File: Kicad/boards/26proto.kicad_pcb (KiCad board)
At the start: 2 copper layers, 17 parts, among them J2 Micro_SD_Card, J3 Conn_01x04, J4 Conn_01x04, U1 MOUDLE-SEEEDUINO-XIAO-ESP32C3, U2 MAX3485, U4 MAX3485, U6 MAX3485, U9 MAX3485

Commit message: update sch
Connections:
- U1 pad 3: unconnected-(U1-GPIO4_A2_D2-Pad3) -> RES
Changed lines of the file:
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@@
 	(net 14 "Pot_trim")
 	(net 15 "SDA_board3")
-	(net 16 "unconnected-(U1-GPIO4_A2_D2-Pad3)")
+	(net 16 "RES")
 	(net 17 "unconnected-(U1-MTDI-Pad17)")
 	(net 18 "SDA-MOSI")
@@
 			(layers "F.Cu" "F.Mask" "F.Paste")
 			(roundrect_rratio 0.25)
-			(net 16 "unconnected-(U1-GPIO4_A2_D2-Pad3)")
+			(net 16 "RES")
 			(pinfunction "GPIO4_A2_D2")
-			(pintype "passive+no_connect")
+			(pintype "passive")
 			(thermal_bridge_angle 45)
 		)

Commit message: updated sch
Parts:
- added J1: 5051104096, footprints:CON_5051104096_MOL, F.Cu at (108.5, 62.8)
- added U11: MOUDLE-SEEEDUINO-XIAO-ESP32C3, footprints:XIAO-ESP32C3-SMD, F.Cu at (62.3, 12.8)
- added U5: MOUDLE-SEEEDUINO-XIAO-ESP32C3, footprints:XIAO-ESP32C3-SMD, F.Cu at (22.2, 12.8)
- added U7: MOUDLE-SEEEDUINO-XIAO-ESP32C3, footprints:XIAO-ESP32C3-SMD, F.Cu at (42.2, 12.8)
- J2: footprint Connector_Card:microSD_HC_Hirose_DM3D-SF -> Connector_Card:microSD_HC_Hirose_DM3AT-SF-PEJM5
- J4: footprint Connector_JST:JST_XH_B3B-XH-A_1x03_P2.50mm_Vertical -> Connector_JST:JST_XH_B4B-XH-A_1x04_P2.50mm_Vertical
- U1: footprint RF_Module:MCU_Seeed_ESP32C3 -> footprints:XIAO-ESP32C3-SMD
- U10: footprint Connector_PinHeader_2.54mm:PinHeader_1x07_P2.54mm_Vertical -> Connector_JST:JST_XH_B7B-XH-A_1x07_P2.50mm_Vertical
- U8: footprint Connector_PinHeader_2.54mm:PinHeader_1x06_P2.54mm_Vertical -> Connector_JST:JST_XH_B6B-XH-A_1x06_P2.50mm_Vertical
- moved U10 21.0 mm to (53.0, 72.5)
- moved J2 18.3 mm to (36.5, 68.5)
- moved U1 10.4 mm to (45.5, 40.0)
- moved U8 7.90 mm to (98.0, 37.0)

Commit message: edited pcb
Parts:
- added J5: RS485_TFT, Connector_JST:JST_XH_S4B-XH-SM4-TB_1x04-1MP_P2.50mm_Horizontal, F.Cu at (134.4, 23.4)
- added J6: RS485_airdata, Connector_JST:JST_XH_S4B-XH-SM4-TB_1x04-1MP_P2.50mm_Horizontal, F.Cu at (134.4, 36.5)
- added J7: RS485_logger_2, Connector_JST:JST_XH_S4B-XH-SM4-TB_1x04-1MP_P2.50mm_Horizontal, F.Cu at (130.5, 134.0)
- added J8: RS485_logger, Connector_JST:JST_XH_S4B-XH-SM4-TB_1x04-1MP_P2.50mm_Horizontal, F.Cu at (127.5, 98.5)
- added J9: BNO085, footprints:MODULE_4754, F.Cu at (108.1, 128.3)
- added R4: R, Resistor_SMD:R_0201_0603Metric_Pad0.64x0.40mm_HandSolder, F.Cu at (144.7, 17.8)
- added R5: R, Resistor_SMD:R_0201_0603Metric_Pad0.64x0.40mm_HandSolder, F.Cu at (144.7, 19.6)
- AS5600: renamed from U8; value ~ -> AS5600 breakout board; footprint Connector_JST:JST_XH_B6B-XH-A_1x06_P2.50mm_Vertical -> Connector_PinHeader_2.54mm:PinHeader_1x06_P2.54mm_Vertical
- DPS310: renamed from U10; value ~ -> Adafruit DPS310; footprint Connector_JST:JST_XH_B7B-XH-A_1x07_P2.50mm_Vertical -> Connector_PinHeader_2.54mm:PinHeader_1x07_P2.54mm_Vertical
- J3: value Conn_01x04 -> URM37; footprint Connector_JST:JST_XH_B4B-XH-A_1x04_P2.50mm_Vertical -> Connector_JST:JST_XH_S4B-XH-SM4-TB_1x04-1MP_P2.50mm_Horizontal
- J4: value Conn_01x04 -> RE12A; footprint Connector_JST:JST_XH_B4B-XH-A_1x04_P2.50mm_Vertical -> Connector_JST:JST_XH_S4B-XH-SM4-TB_1x04-1MP_P2.50mm_Horizontal
- RV1, RV2, RV3: footprint Connector_JST:JST_XH_B3B-XH-A_1x03_P2.50mm_Vertical -> Connector_JST:JST_XH_S3B-XH-SM4-TB_1x03-1MP_P2.50mm_Horizontal
- U1: value MOUDLE-SEEEDUINO-XIAO-ESP32C3 -> MOUDLE-SEEEDUINO-XIAO-ESP32C3_TFT
- U11: value MOUDLE-SEEEDUINO-XIAO-ESP32C3 -> MOUDLE-SEEEDUINO-XIAO-ESP32C3_pot
- U5: value MOUDLE-SEEEDUINO-XIAO-ESP32C3 -> MOUDLE-SEEEDUINO-XIAO-ESP32C3_logger
- U7: value MOUDLE-SEEEDUINO-XIAO-ESP32C3 -> MOUDLE-SEEEDUINO-XIAO-ESP32C3_airdata
- moved RV3 148.1 mm to (218.8, 54.5)
- moved J3 142.0 mm to (212.8, 37.2)
- moved U11 132.2 mm to (192.0, 38.5)
- moved RV2 132.2 mm to (203.0, 57.5)
- moved U7 131.2 mm to (171.0, 38.0)
- moved U5 125.0 mm to (107.3, 104.4)
- moved RV1 117.3 mm to (187.5, 58.5)
- moved J2 105.4 mm to (129.5, 118.0), turned to 90 degrees
- moved J1 55.7 mm to (163.5, 54.5), turned to 180 degrees
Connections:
- AS5600 pad 1: (no net) -> unconnected-(AS5600-5V-Pad1)
- AS5600 pad 2: (no net) -> +3.3V
- AS5600 pad 3: (no net) -> GND
- AS5600 pad 4: (no net) -> SCL_airdata
- AS5600 pad 5: (no net) -> SDA_aridata
- AS5600 pad 6: (no net) -> unconnected-(AS5600-OUT-Pad6)
- DPS310 pad 1: (no net) -> unconnected-(DPS310-VIN-Pad1)
- DPS310 pad 2: (no net) -> +3.3V
- DPS310 pad 3: (no net) -> GND
- DPS310 pad 4: (no net) -> SCL_airdata
- DPS310 pad 5: (no net) -> GND
- DPS310 pad 6: (no net) -> SDA_aridata
- DPS310 pad 7: (no net) -> +3.3V
- U11 pad 11: Net-(U11-GPIO10_D10_MOSI) -> unconnected-(U11-GPIO10_D10_MOSI-Pad11)
- U11 pad 7: Net-(U11-GPIO21_D6_TX) -> unconnected-(U11-GPIO21_D6_TX-Pad7)
- U11 pad 8: Net-(U11-GPIO20_D7_RX) -> unconnected-(U11-GPIO20_D7_RX-Pad8)

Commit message: edited sch and pcb
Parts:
- added Q2: NPN, Package_TO_SOT_SMD:SOT-23, F.Cu at (126.6, 79.0)
- added R6: R, Resistor_SMD:R_0201_0603Metric_Pad0.64x0.40mm_HandSolder, F.Cu at (43.6, 104.5)
- added R7: R, Resistor_SMD:R_0201_0603Metric_Pad0.64x0.40mm_HandSolder, F.Cu at (43.6, 106.2)
- added R8: R, Resistor_SMD:R_0201_0603Metric_Pad0.64x0.40mm_HandSolder, F.Cu at (43.6, 108.0)
- moved J6 103.4 mm to (57.5, 105.5), turned to 180 degrees
- moved R4 82.6 mm to (65.6, 41.5)
- moved C1 75.7 mm to (119.1, 105.0)
- moved R1 75.7 mm to (119.1, 106.8)
- moved R2 75.7 mm to (119.1, 108.5)
- moved R3 75.7 mm to (119.1, 110.2)
- moved AS5600 72.0 mm to (43.0, 83.4)
- moved J5 54.6 mm to (168.1, 66.5), turned to 180 degrees
- moved U1 48.8 mm to (57.0, 87.4), turned to -90 degrees
- moved R5 35.2 mm to (153.9, 53.5)
- moved J3 34.1 mm to (231.0, 66.0), turned to 180 degrees
- moved J4 31.6 mm to (57.0, 66.5)
- moved DPS310 14.6 mm to (43.0, 61.9)
- moved RV3 12.6 mm to (214.5, 66.2), turned to 180 degrees
- moved J1 10.0 mm to (173.5, 55.5), turned to 0 degrees
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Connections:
- AS5600 pad 2: +3.3V -> encoder_anode
- AS5600 pad 3: GND -> encoder_cathode
- C1 pad 1: +3.3V -> encoder_anode
- C1 pad 2: GND -> encoder_cathode
- DPS310 pad 2: +3.3V -> encoder_anode
- DPS310 pad 3: GND -> encoder_cathode
- DPS310 pad 5: GND -> encoder_cathode
- DPS310 pad 7: +3.3V -> encoder_anode
- J1 pad 1: GND -> encoder_cathode
- J1 pad 31: GND -> encoder_cathode
- J1 pad 32: +3.3V -> encoder_anode
- J1 pad 33: +3.3V -> encoder_anode
- J1 pad 34: GND -> encoder_cathode
- J1 pad 35: GND -> encoder_cathode
- J1 pad 36: GND -> encoder_cathode
- J1 pad 37: GND -> encoder_cathode
- J1 pad 39: GND -> encoder_cathode
- J1 pad 7: +3.3V -> encoder_anode
- J1 pad 8: +3.3V -> encoder_anode
- J2 pad 4: +3.3V -> encoder_anode
- J2 pad 6: GND -> encoder_cathode
- J2 pad 9: GND -> encoder_cathode
- J3 pad 1: +3.3V -> encoder_anode
- J3 pad 2: GND -> encoder_cathode
- J4 pad 1: +3.3V -> Net-(J4-Pin_1)
- J4 pad 2: GND -> encoder_raw
- J4 pad 3: Encoder_Apin -> encoder_cathode
- J4 pad 4: Encoder_Bpin -> encoder_cathode
- J5 pad 2: GND -> encoder_cathode
- J6 pad 2: GND -> encoder_cathode
- J7 pad 2: GND -> encoder_cathode
- J8 pad 2: GND -> encoder_cathode
- R1 pad 2: +3.3V -> encoder_anode
- R2 pad 2: +3.3V -> encoder_anode
- R3 pad 2: +3.3V -> encoder_anode
- RV1 pad 1: GND -> encoder_cathode
- RV1 pad 3: +3.3V -> encoder_anode
- RV2 pad 1: GND -> encoder_cathode
- RV2 pad 3: +3.3V -> encoder_anode
- RV3 pad 1: GND -> encoder_cathode
- RV3 pad 3: +3.3V -> encoder_anode
- U1 pad 12: +3.3V -> encoder_anode
- U1 pad 13: GND -> encoder_cathode
- U1 pad 16: GND -> encoder_cathode
- U11 pad 12: +3.3V -> encoder_anode
- U11 pad 13: GND -> encoder_cathode
- U11 pad 16: GND -> encoder_cathode
- U2 pad 5: GND -> encoder_cathode
- U2 pad 8: +3.3V -> encoder_anode
- U4 pad 5: GND -> encoder_cathode
- U4 pad 8: +3.3V -> encoder_anode
- U5 pad 12: +3.3V -> encoder_anode
- U5 pad 13: GND -> encoder_cathode
- U5 pad 16: GND -> encoder_cathode
- U6 pad 5: GND -> encoder_cathode
- U6 pad 8: +3.3V -> encoder_anode
- U7 pad 10: Encoder_Apin -> encoder_out
- U7 pad 12: +3.3V -> encoder_anode
- U7 pad 13: GND -> encoder_cathode
- U7 pad 16: GND -> encoder_cathode
- U7 pad 9: Encoder_Bpin -> unconnected-(U7-GPIO8_D8_SCK-Pad9)

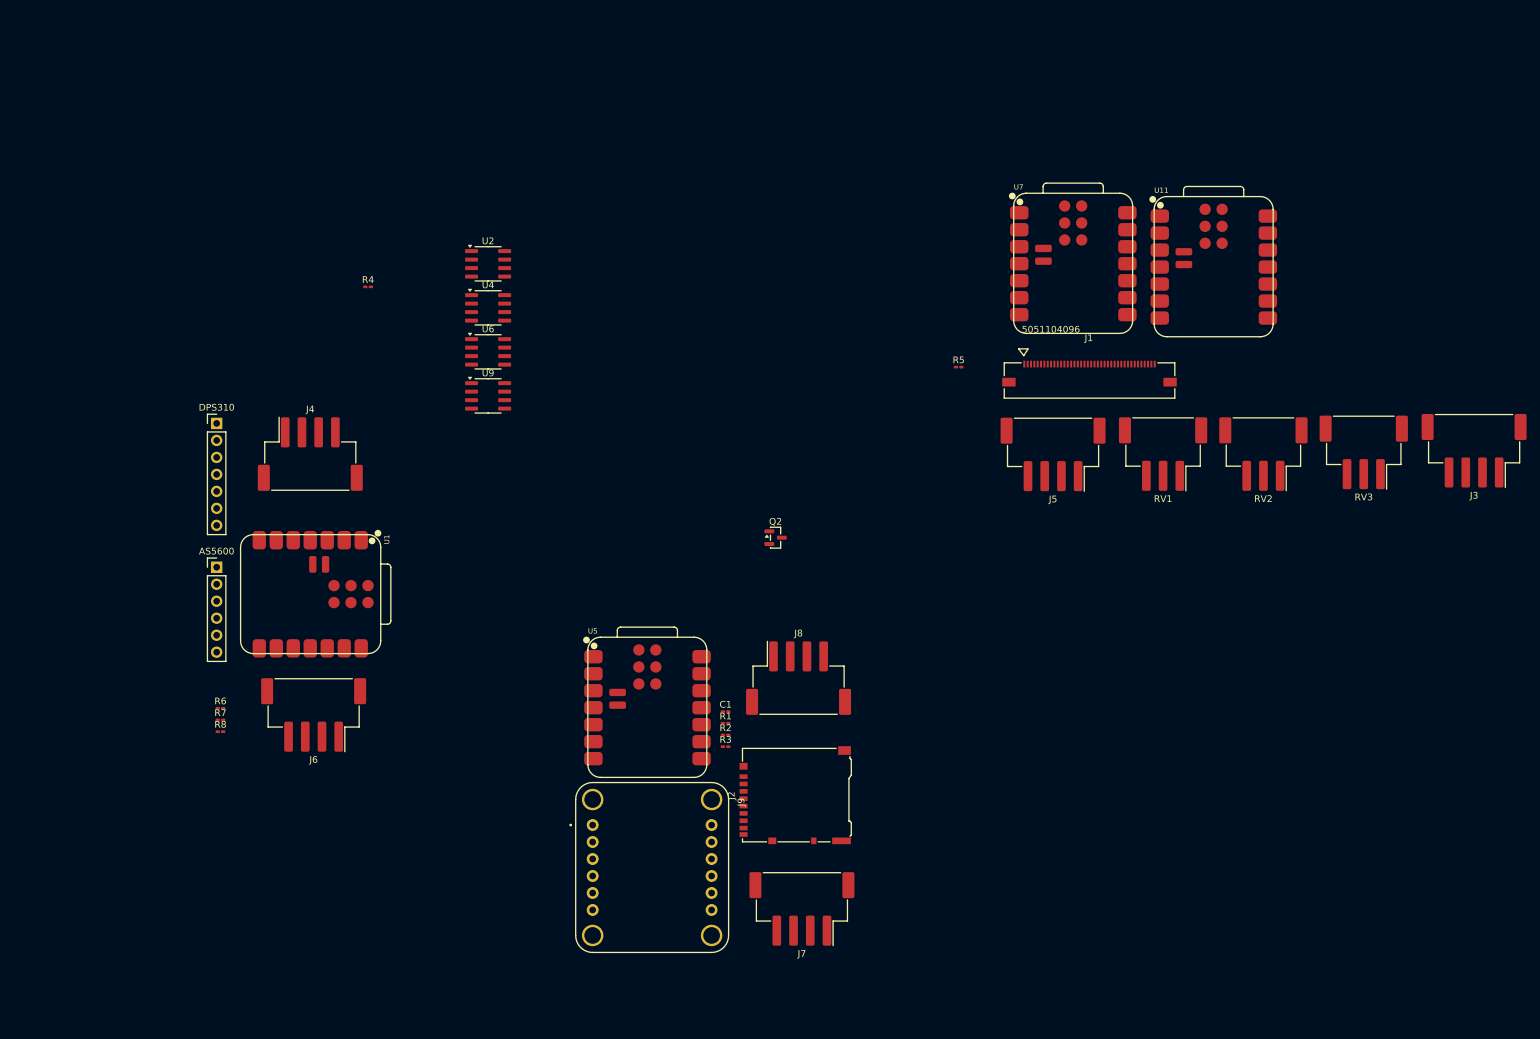
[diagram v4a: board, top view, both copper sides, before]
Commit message: Add battery connector and update net assignments
Added Batt1 JST PH connector footprint and R4 resistor for RS485 lines. Updated net assignments for U11 pins, replaced encoder_anode with +3.3V and pot_Vin where appropriate, and made related schematic and PCB changes. Also added a backup ZIP file.
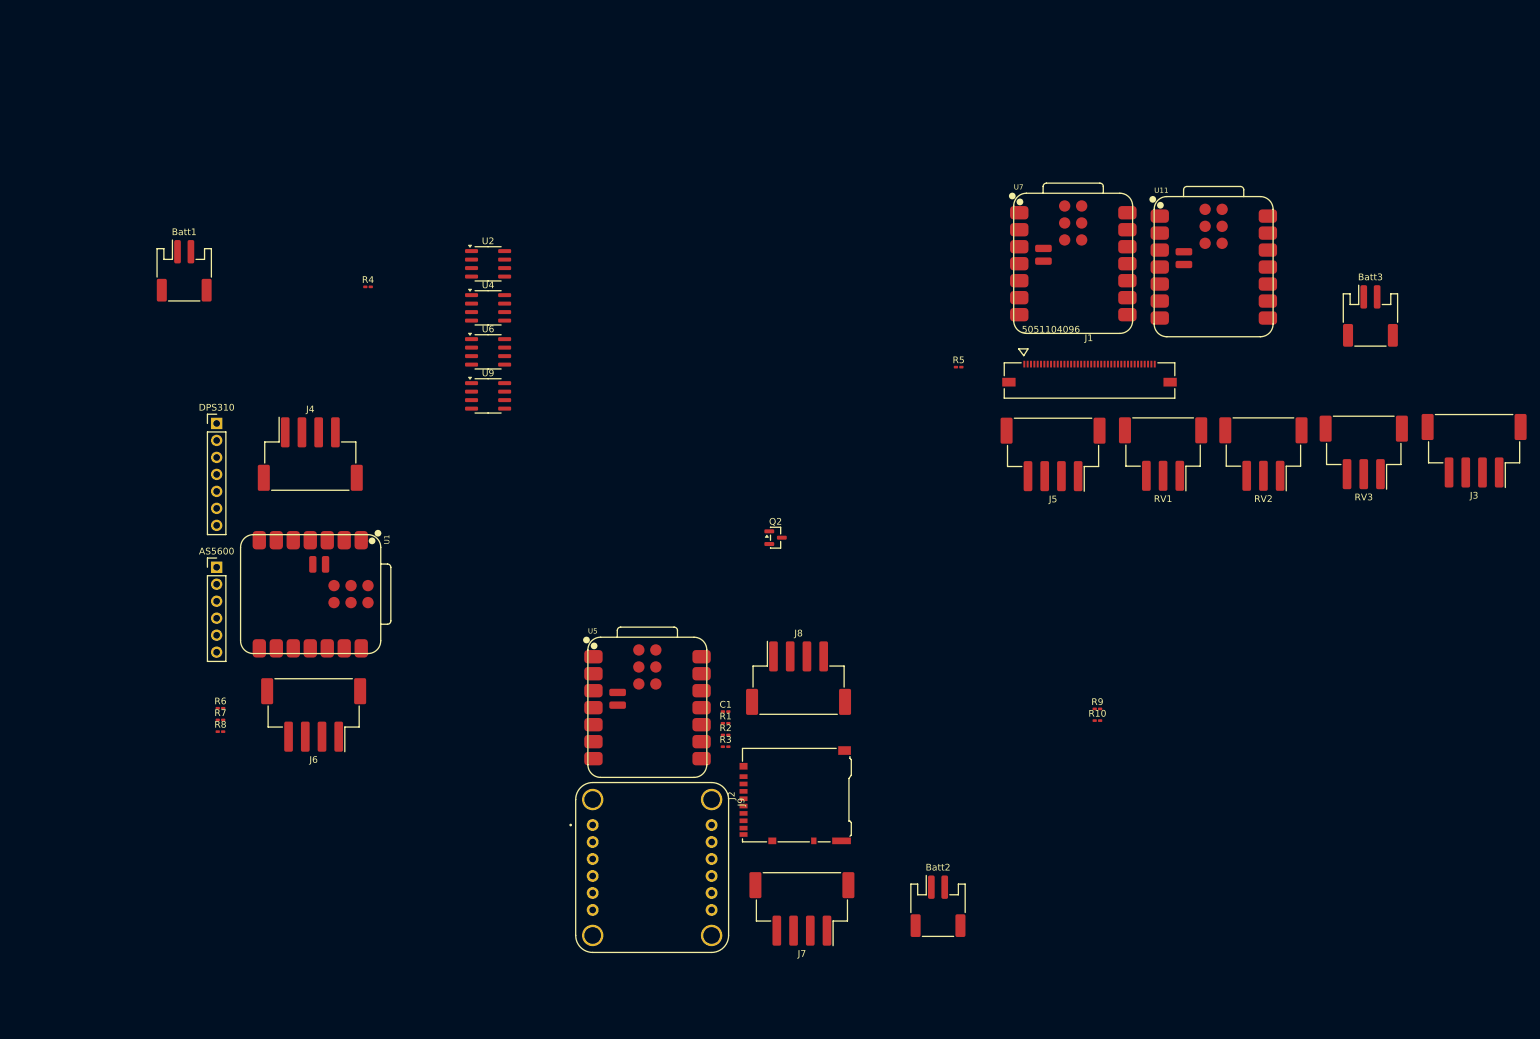
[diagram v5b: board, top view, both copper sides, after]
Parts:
- added Batt1: Conn_01x02, Connector_JST:JST_PH_S2B-PH-SM4-TB_1x02-1MP_P2.00mm_Horizontal, F.Cu at (38.1, 39.1)
- added Batt2: Conn_01x02, Connector_JST:JST_PH_S2B-PH-SM4-TB_1x02-1MP_P2.00mm_Horizontal, F.Cu at (150.8, 134.1)
- added Batt3: Conn_01x02, Connector_JST:JST_PH_S2B-PH-SM4-TB_1x02-1MP_P2.00mm_Horizontal, F.Cu at (215.5, 45.9)
- added R10: R, Resistor_SMD:R_0201_0603Metric_Pad0.64x0.40mm_HandSolder, F.Cu at (174.7, 106.3)
- added R9: R, Resistor_SMD:R_0201_0603Metric_Pad0.64x0.40mm_HandSolder, F.Cu at (174.7, 104.6)
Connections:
- AS5600 pad 2: encoder_anode -> +3.3V
- C1 pad 1: encoder_anode -> +3.3V
- DPS310 pad 2: encoder_anode -> +3.3V
- DPS310 pad 7: encoder_anode -> +3.3V
- J1 pad 32: encoder_anode -> +3.3V
- J1 pad 33: encoder_anode -> +3.3V
- J1 pad 7: encoder_anode -> +3.3V
- J1 pad 8: encoder_anode -> +3.3V
- J2 pad 4: encoder_anode -> +3.3V
- J3 pad 1: encoder_anode -> +3.3V
- Q2 pad 1: Net-(Q2-C) -> encoder_out
- Q2 pad 3: encoder_out -> encoder_cathode
- R1 pad 2: encoder_anode -> +3.3V
- R2 pad 2: encoder_anode -> +3.3V
- R3 pad 2: encoder_anode -> +3.3V
- R6 pad 1: encoder_anode -> +3.3V
- R6 pad 2: Net-(Q2-C) -> encoder_out
- RV1 pad 3: encoder_anode -> pot_Vin
- RV2 pad 3: encoder_anode -> pot_Vin
- RV3 pad 3: encoder_anode -> pot_Vin
- U1 pad 12: encoder_anode -> +3.3V
- U11 pad 10: RX_URM37 -> unconnected-(U11-GPIO9_D9_MISO-Pad10)
- U11 pad 12: encoder_anode -> +3.3V
- U11 pad 7: unconnected-(U11-GPIO21_D6_TX-Pad7) -> TX_URM37
- U11 pad 8: unconnected-(U11-GPIO20_D7_RX-Pad8) -> RX_URM37
- U11 pad 9: TX_URM37 -> unconnected-(U11-GPIO8_D8_SCK-Pad9)
- U2 pad 8: encoder_anode -> +3.3V
- U4 pad 8: encoder_anode -> +3.3V
- U5 pad 12: encoder_anode -> +3.3V
- U6 pad 8: encoder_anode -> +3.3V
- U7 pad 12: encoder_anode -> +3.3V

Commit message: updated TFT and sensors board
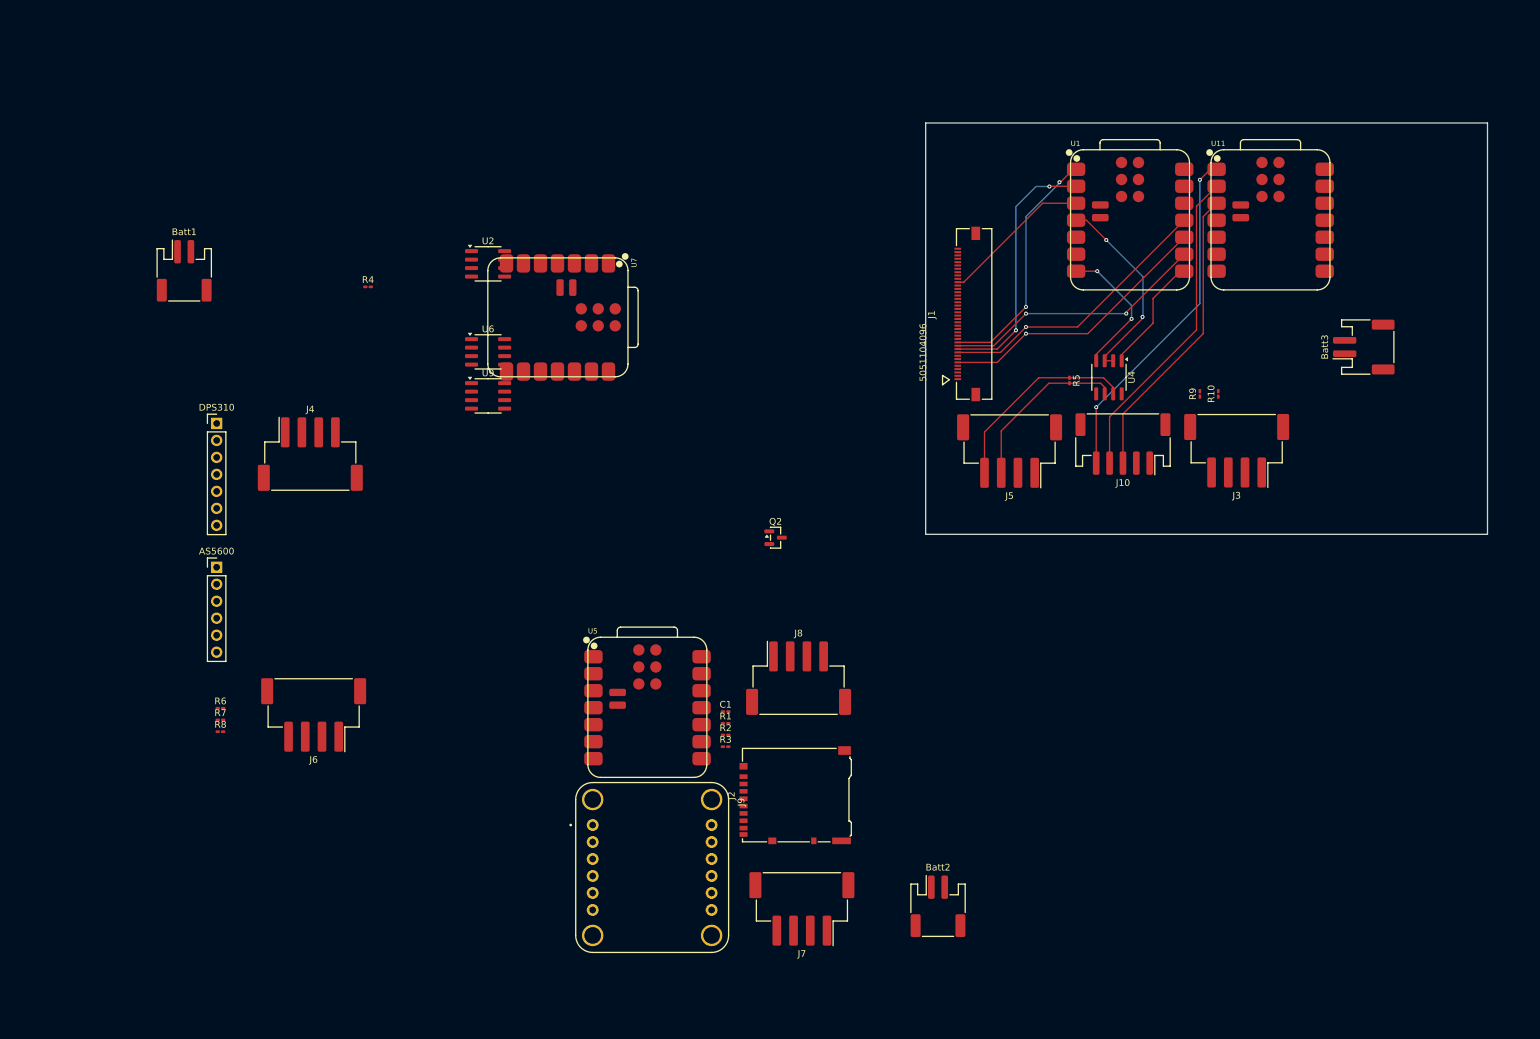
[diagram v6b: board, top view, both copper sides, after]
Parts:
- removed RV1, RV2, RV3: R_Potentiometer, Connector_JST:JST_XH_S3B-XH-SM4-TB_1x03-1MP_P2.50mm_Horizontal
- added J10: Conn_01x05, Connector_JST:JST_PH_S5B-PH-SM4-TB_1x05-1MP_P2.00mm_Horizontal, F.Cu at (178.5, 65.0)
- moved U1 134.6 mm to (179.5, 31.5), turned to 0 degrees
- moved U4 93.4 mm to (176.4, 55.0), turned to -90 degrees
- moved U7 77.4 mm to (94.0, 46.0), turned to -90 degrees
- moved R10 52.1 mm to (192.8, 57.5), turned to 90 degrees
- moved R9 49.5 mm to (190.0, 57.5), turned to 90 degrees
- moved J3 35.5 mm to (195.5, 66.0)
- moved J1 19.9 mm to (156.2, 45.5), turned to 90 degrees
- moved R5 16.7 mm to (170.5, 55.5), turned to -90 degrees
- moved U11 11.0 mm to (200.5, 31.5)
- moved J5 6.52 mm to (161.6, 66.0)
- moved Batt3 4.76 mm to (214.5, 50.5), turned to 90 degrees
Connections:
- U1 pad 1: CS -> WRX-D/C
- U1 pad 2: WRX-D/C -> CS
- U11 pad 1: Pot_elv -> Pot_trim
- U11 pad 3: Pot_trim -> Pot_elv
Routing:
- net Pot_trim: track 0.00 -> 51.9 mm, vias 0 -> 2
- net Pot_rud: track 0.00 -> 48.0 mm
- net Pot_elv: track 0.00 -> 44.6 mm
- net SDA-MOSI: track 0.00 -> 42.0 mm, vias 0 -> 1
- net SDO-MISO: track 0.00 -> 41.6 mm, vias 0 -> 1
- net DCX-SCLK: track 0.00 -> 39.7 mm, vias 0 -> 2
- net CS: track 0.00 -> 38.6 mm, vias 0 -> 2
- net WRX-D/C: track 0.00 -> 36.4 mm, vias 0 -> 2
- net RS485_B: track 0.00 -> 30.3 mm
- net Net-(U1-GPIO5_A3_D3): track 0.00 -> 29.8 mm, vias 0 -> 2
- net RS485_A: track 0.00 -> 25.9 mm
- net RES: track 0.00 -> 22.6 mm
- net Net-(U1-GPIO21_D6_TX): track 0.00 -> 20.9 mm, vias 0 -> 2
- net Net-(U1-GPIO20_D7_RX): track 0.00 -> 17.6 mm
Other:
- board outline added: 84 x 61.5 mm
